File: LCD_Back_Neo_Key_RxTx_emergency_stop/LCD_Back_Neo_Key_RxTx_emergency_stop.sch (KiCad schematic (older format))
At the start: 12 parts, among them J1 Screw_Terminal_01x09, J2 Conn_01x20_Female, J3 Conn_01x08_Male, J4 Conn_01x01_Female, J5 Conn_01x01_Female, Q1 BC337, U1 DC-DC_Stepdown-Zimprich

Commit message: add new sheet 'Display'
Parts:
- removed C1: CP, Capacitor_THT:CP_Radial_D8.0mm_P2.50mm, symbol Device:CP
- removed J2: Conn_01x20_Female, Connector:LcdPinHeader, symbol LCD_Back_Neo_Key_RxTx_emergency_stop-rescue:Conn_01x20_LCD-Connector-ArduinoSig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
- removed Q1: BC337, Package_TO_SOT_THT:TO-92_Inline, symbol Transistor_BJT:BC337
- removed R1: R, Resistor_THT:R_Axial_DIN0207_L6.3mm_D2.5mm_P15.24mm_Horizontal, symbol Device:R
- removed R2: R, Resistor_THT:R_Axial_DIN0207_L6.3mm_D2.5mm_P10.16mm_Horizontal, symbol Device:R
- removed RL1: SONGLE_Relay_SRU-12VDC-SL-C, Relays_ThroughHole:Relay_SANYOU_SRD_Series_Form_C, symbol Zimprich:SONGLE_Relay_SRU-12VDC-SL-C
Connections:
- wire segments 60 -> 41
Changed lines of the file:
@@
 $Descr A4 11693 8268
 encoding utf-8
-Sheet 1 1
+Sheet 1 2
 Title ""
 Date "sam. 04 avril 2015"
@@
 	-1   0    0    1
 $EndComp
-$Comp
-L LCD_Back_Neo_Key_RxTx_emergency_stop-rescue:Conn_01x20_LCD-Connector-ArduinoSignalDriver-rescue J2
-U 1 1 5CE064F0
-P 9400 2150
-F 0 "J2" V 9565 2080 50  0000 C CNN
-F 1 "Conn_01x20_Female" V 9474 2080 50  0000 C CNN
-F 2 "Connector:LcdPinHeader" H 9400 2150 50  0001 C CNN
-F 3 "~" H 9400 2150 50  0001 C CNN
-	1    9400 2150
-	0    -1   -1   0
-$EndComp
-Text GLabel 10400 3550 3    50   Input ~ 0
-GND
-Text GLabel 10300 3550 3    50   Input ~ 0
-VCC-5V
-$Comp
-L Device:CP C1
-U 1 1 5CE0A632
-P 10200 4200
-F 0 "C1" H 10318 4246 50  0000 L CNN
-F 1 "CP" H 10318 4155 50  0000 L CNN
-F 2 "Capacitor_THT:CP_Radial_D8.0mm_P2.50mm" H 10238 4050 50  0001 C CNN
-F 3 "~" H 10200 4200 50  0001 C CNN
-	1    10200 4200
-	1    0    0    -1
-$EndComp
-$Comp
-L Device:R R1
-U 1 1 5CE0B53A
-P 9850 4050
-F 0 "R1" V 9643 4050 50  0000 C CNN
-F 1 "R" V 9734 4050 50  0000 C CNN
-F 2 "Resistor_THT:R_Axial_DIN0207_L6.3mm_D2.5mm_P15.24mm_Horizontal" V 9735 4050 50  0001 C CNN
-F 3 "~" H 9850 4050 50  0001 C CNN
-	1    9850 4050
-	0    1    1    0
-$EndComp
-Text GLabel 10200 4550 3    50   Input ~ 0
-GND
-Wire Wire Line
-	10200 4550 10200 4350
-Wire Wire Line
-	10000 4050 10200 4050
-Text GLabel 9500 4050 0    50   Input ~ 0
-Ardu_D3
-Wire Wire Line
-	9500 4050 9700 4050
 Wire Wire Line
 	5300 3100 5300 3650
@@
 Text GLabel 2200 4250 0    50   Input ~ 0
 GND
-$Comp
-L Transistor_BJT:BC337 Q1
-U 1 1 5CE3D215
-P 8400 4050
-F 0 "Q1" H 8591 4096 50  0000 L CNN
-F 1 "BC337" H 8591 4005 50  0000 L CNN
-F 2 "Package_TO_SOT_THT:TO-92_Inline" H 8600 3975 50  0001 L CIN
-F 3 "https://diotec.com/tl_files/diotec/files/pdf/datasheets/bc337.pdf" H 8400 4050 50  0001 L CNN
-	1    8400 4050
-	1    0    0    -1
-$EndComp
-$Comp
-L Device:R R2
-U 1 1 5CE41104
-P 7800 4050
-F 0 "R2" V 7593 4050 50  0000 C CNN
-F 1 "R" V 7684 4050 50  0000 C CNN
-F 2 "Resistor_THT:R_Axial_DIN0207_L6.3mm_D2.5mm_P10.16mm_Horizontal" V 7685 4050 50  0001 C CNN
-F 3 "~" H 7800 4050 50  0001 C CNN
-	1    7800 4050
-	0    1    1    0
-$EndComp
-Wire Wire Line
-	7950 4050 8200 4050
-Text GLabel 7350 4050 0    50   Input ~ 0
-Ardu_D5
-Wire Wire Line
-	7350 4050 7650 4050
-Text GLabel 8500 4350 3    50   Input ~ 0
-GND
-Wire Wire Line
-	8500 4350 8500 4250
-Wire Wire Line
-	8600 3400 10300 3400
-Wire Wire Line
-	10200 2350 10200 4050
-Connection ~ 10200 4050
-Wire Wire Line
-	8500 2350 8500 3850
-Wire Wire Line
-	10400 2350 10400 3300
-Connection ~ 10300 3400
-Wire Wire Line
-	10300 3400 10300 3550
-Wire Wire Line
-	10300 2350 10300 3400
-Wire Wire Line
-	8600 2350 8600 3400
-Wire Wire Line
-	9000 3300 10400 3300
-Wire Wire Line
-	9000 2350 9000 3300
-Connection ~ 10400 3300
-Wire Wire Line
-	10400 3300 10400 3550
 Text GLabel 6200 4650 2    50   Input ~ 0
 Ardu_A0
@@
 Wire Wire Line
 	4700 5350 4900 5350
-Text GLabel 10100 2550 3    50   Input ~ 0
-Ardu_A0
-Text GLabel 10000 2550 3    50   Input ~ 0
-Ardu_A1
-Text GLabel 9900 2550 3    50   Input ~ 0
-Ardu_D13
-Wire Wire Line
-	10100 2550 10100 2350
-Wire Wire Line
-	10000 2550 10000 2350
-Wire Wire Line
-	9900 2550 9900 2350
 Wire Wire Line
 	1050 4350 2350 4350
@@
 	1    0    0    -1
 $EndComp
-$Comp
-L Zimprich:SONGLE_Relay_SRU-12VDC-SL-C RL1
-U 1 1 5CE2CEAB
-P 3750 2300
-F 0 "RL1" H 4380 2546 50  0000 L CNN
-F 1 "SONGLE_Relay_SRU-12VDC-SL-C" H 4380 2455 50  0000 L CNN
-F 2 "Relays_ThroughHole:Relay_SANYOU_SRD_Series_Form_C" H 4400 2450 50  0001 L CNN
-F 3 "https://www.omron.com/ecb/products/pdf/en-g5q.pdf" H 3950 2100 50  0001 C CNN
-	1    3750 2300
-	1    0    0    -1
-$EndComp
+$Sheet
+S 9950 750  1050 250
+U 5CED8FBC
+F0 "Display" 50
+F1 "display.sch" 50
+$EndSheet
 $EndSCHEMATC

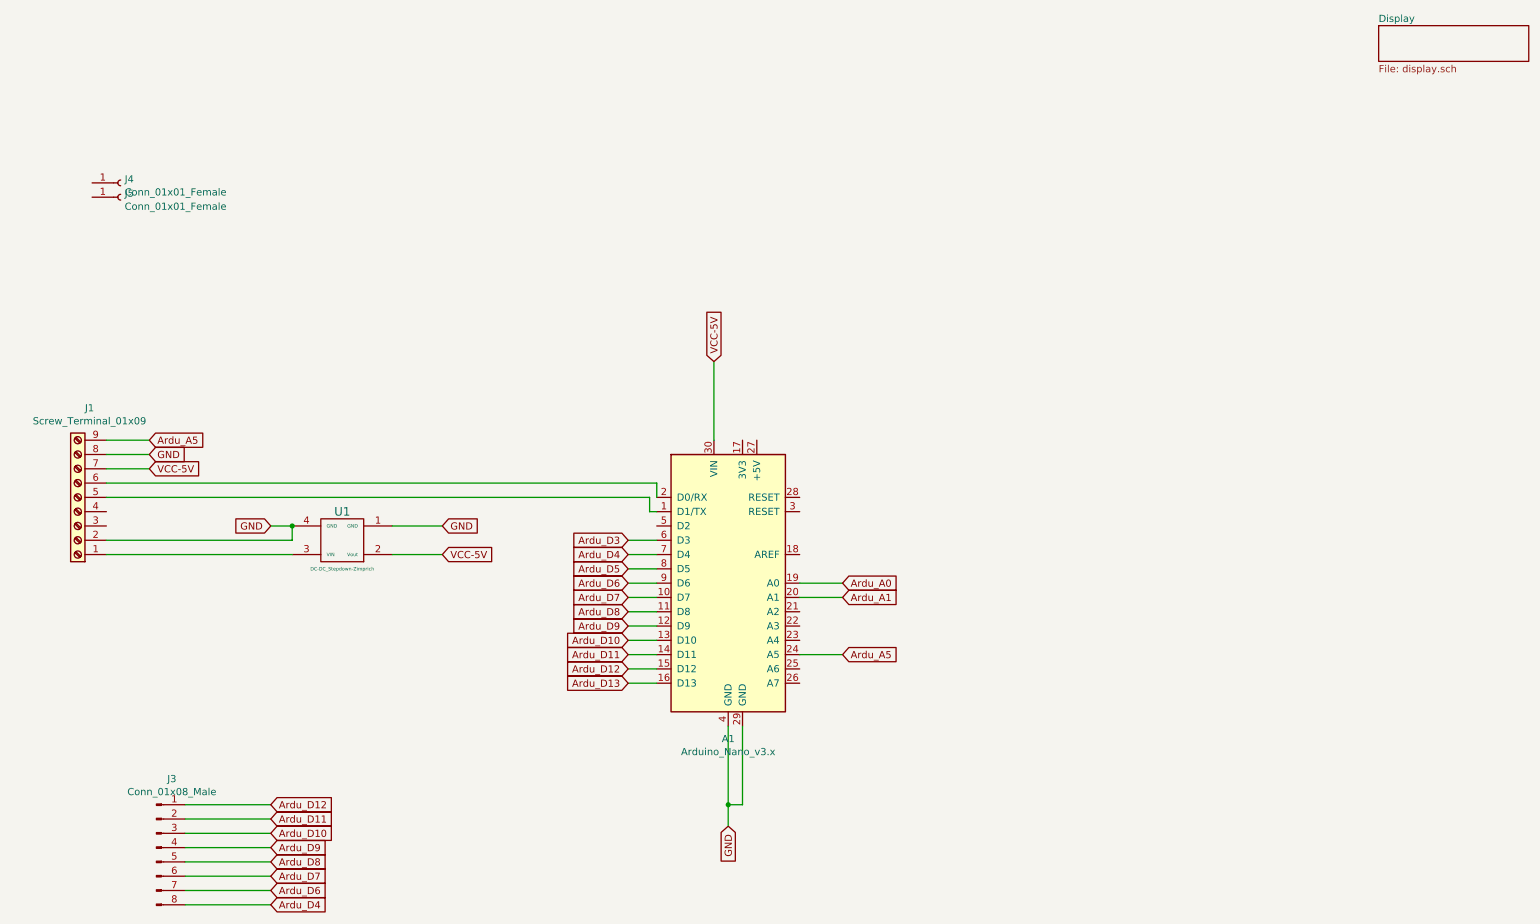
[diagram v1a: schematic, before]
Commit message: add sheet for emergency stop
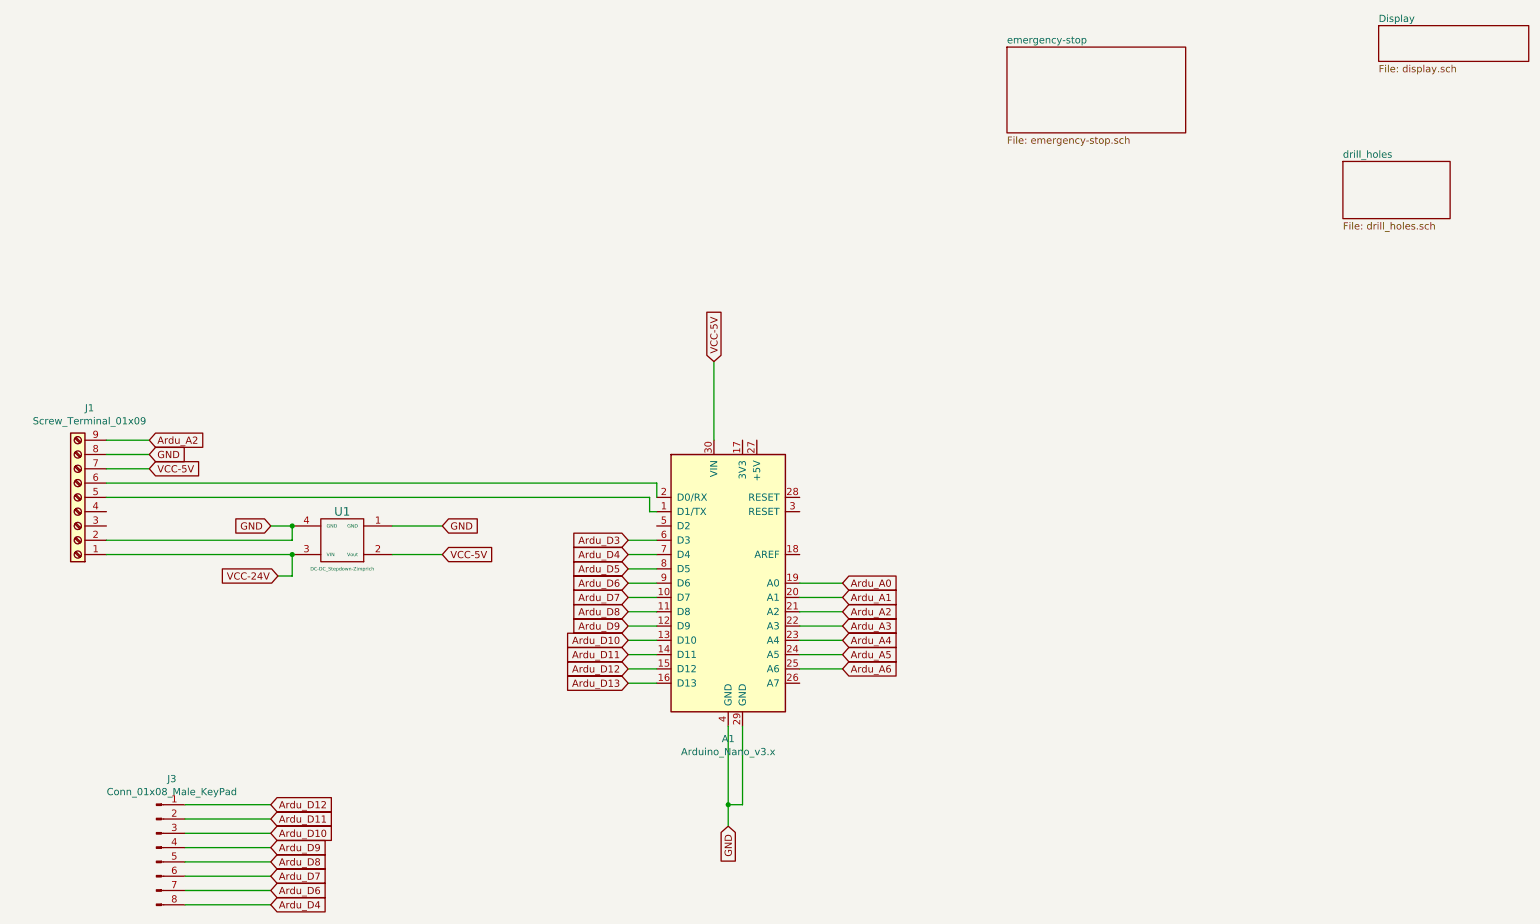
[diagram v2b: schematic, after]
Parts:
- removed J4, J5: Conn_01x01_Female, Connector_Pin:Pin_D0.7mm_L6.5mm_W1.8mm_FlatFork, symbol Connector:Conn_01x01_Female
- J3: value Conn_01x08_Male -> Conn_01x08_Male_KeyPad
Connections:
- net Ardu_A5: no longer J1.9 (Pin_9)
- net VCC-24V: now reaches J1.1 (Pin_1), U1.3 (VIN)
- net Ardu_A2: now reaches A1.21 (A2)
- net Ardu_A2: now also J1.9 (Pin_9)
- net Ardu_A3: now reaches A1.22 (A3)
- net Ardu_A4: now reaches A1.23 (A4)
- net Ardu_A6: now reaches A1.25 (A6)
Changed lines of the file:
@@
 $Descr A4 11693 8268
 encoding utf-8
-Sheet 1 2
+Sheet 1 4
 Title ""
 Date "sam. 04 avril 2015"
@@
 Wire Wire Line
 	5400 6200 5400 6350
-Text GLabel 6200 5150 2    50   Input ~ 0
-Ardu_A5
-Wire Wire Line
-	6200 5150 5900 5150
+Text GLabel 6200 4850 2    50   Input ~ 0
+Ardu_A2
 Text GLabel 1350 3650 2    50   Input ~ 0
-Ardu_A5
+Ardu_A2
 Wire Wire Line
 	1050 3650 1350 3650
@@
 P 1400 6500
 F 0 "J3" H 1508 6981 50  0000 C CNN
-F 1 "Conn_01x08_Male" H 1508 6890 50  0000 C CNN
+F 1 "Conn_01x08_Male_KeyPad" H 1508 6890 50  0000 C CNN
 F 2 "Connector_PinHeader_2.54mm:PinHeader_1x08_P2.54mm_Horizontal_invert" H 1400 6500 50  0001 C CNN
 F 3 "~" H 1400 6500 50  0001 C CNN
@@
 Wire Wire Line
 	4850 4050 1050 4050
-$Comp
-L Connector:Conn_01x01_Female J4
-U 1 1 5CE84571
-P 1150 1850
-F 0 "J4" H 1178 1876 50  0000 L CNN
-F 1 "Conn_01x01_Female" H 1178 1785 50  0000 L CNN
-F 2 "Connector_Pin:Pin_D0.7mm_L6.5mm_W1.8mm_FlatFork" H 1150 1850 50  0001 C CNN
-F 3 "~" H 1150 1850 50  0001 C CNN
-	1    1150 1850
-	1    0    0    -1
-$EndComp
-$Comp
-L Connector:Conn_01x01_Female J5
-U 1 1 5CE84B70
-P 1150 1950
-F 0 "J5" H 1178 1976 50  0000 L CNN
-F 1 "Conn_01x01_Female" H 1178 1885 50  0000 L CNN
-F 2 "Connector_Pin:Pin_D0.7mm_L6.5mm_W1.8mm_FlatFork" H 1150 1950 50  0001 C CNN
-F 3 "~" H 1150 1950 50  0001 C CNN
-	1    1150 1950
-	1    0    0    -1
-$EndComp
 $Sheet
 S 9950 750  1050 250
@@
 F1 "display.sch" 50
 $EndSheet
+Text GLabel 2250 4600 0    50   Input ~ 0
+VCC-24V
+Wire Wire Line
+	2250 4600 2350 4600
+Wire Wire Line
+	2350 4600 2350 4450
+Connection ~ 2350 4450
+$Sheet
+S 7350 900  1250 600
+U 5CED30A6
+F0 "emergency-stop" 50
+F1 "emergency-stop.sch" 50
+$EndSheet
+Wire Wire Line
+	6200 4850 5900 4850
+Text GLabel 6200 5050 2    50   Input ~ 0
+Ardu_A4
+Text GLabel 6200 5150 2    50   Input ~ 0
+Ardu_A5
+Wire Wire Line
+	6200 5050 5900 5050
+Wire Wire Line
+	6200 5150 5900 5150
+Text GLabel 6200 4950 2    50   Input ~ 0
+Ardu_A3
+Wire Wire Line
+	6200 4950 5900 4950
+$Sheet
+S 9700 1700 750  400
+U 5CF1B710
+F0 "drill_holes" 50
+F1 "drill_holes.sch" 50
+$EndSheet
+Text GLabel 6200 5250 2    50   Input ~ 0
+Ardu_A6
+Wire Wire Line
+	6200 5250 5900 5250
 $EndSCHEMATC

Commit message: combine screw terminal
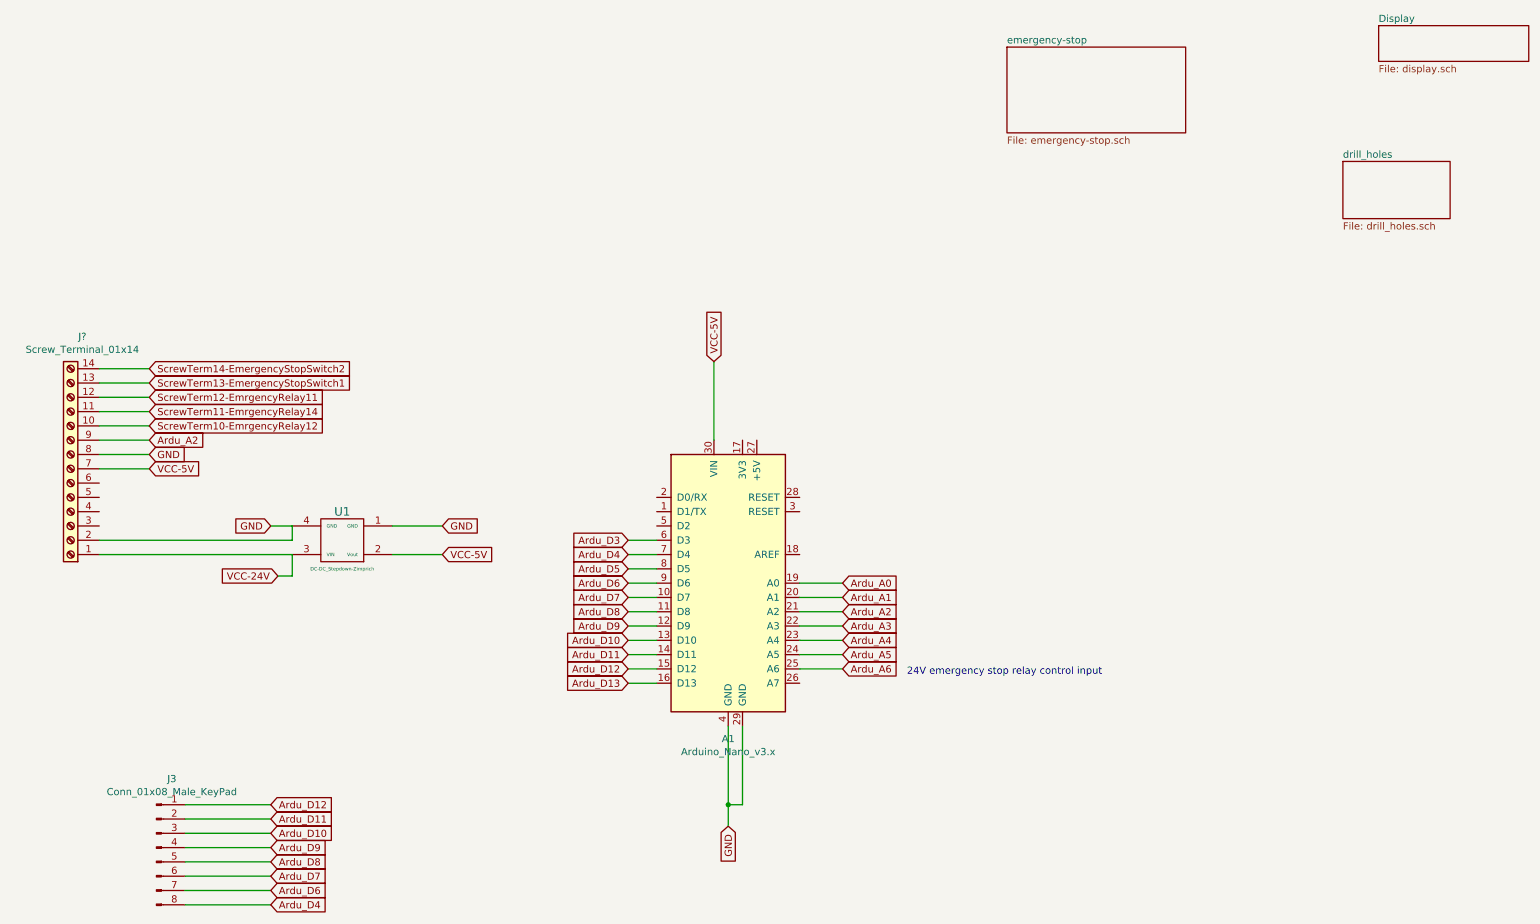
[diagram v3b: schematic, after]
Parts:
- removed J1: Screw_Terminal_01x09, TerminalBlock_Altech:Altech_AK300_1x09_P5.00mm_45-Degree, symbol Connector:Screw_Terminal_01x09
- added J?: Screw_Terminal_01x14, symbol Connector:Screw_Terminal_01x14
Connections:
- net Ardu_A2: now also J?.9 (Pin_9)
- net GND: now also J?.2 (Pin_2), J?.8 (Pin_8)
- net VCC-24V: now also J?.1 (Pin_1)
- net VCC-5V: now also J?.7 (Pin_7)
- new net ScrewTerm10-EmrgencyRelay12: J?.10 (Pin_10)
- new net ScrewTerm11-EmrgencyRelay14: J?.11 (Pin_11)
- new net ScrewTerm12-EmrgencyRelay11: J?.12 (Pin_12)
- new net ScrewTerm13-EmergencyStopSwitch1: J?.13 (Pin_13)
- new net ScrewTerm14-EmergencyStopSwitch2: J?.14 (Pin_14)
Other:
- note added: "24V emergency stop relay control input"
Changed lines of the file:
@@
 Wire Wire Line
 	3050 4450 3400 4450
-$Comp
-L Connector:Screw_Terminal_01x09 J1
-U 1 1 5CDFAC77
-P 850 4050
-F 0 "J1" H 768 3425 50  0000 C CNN
-F 1 "Screw_Terminal_01x09" H 768 3516 50  0000 C CNN
-F 2 "TerminalBlock_Altech:Altech_AK300_1x09_P5.00mm_45-Degree" H 850 4050 50  0001 C CNN
-F 3 "~" H 850 4050 50  0001 C CNN
-	1    850  4050
-	-1   0    0    1
-$EndComp
 Wire Wire Line
 	5300 3100 5300 3650
 Text GLabel 1350 3850 2    50   Input ~ 0
 VCC-5V
-Wire Wire Line
-	1350 3850 1050 3850
 Text GLabel 1350 3750 2    50   Input ~ 0
 GND
-Wire Wire Line
-	1350 3750 1050 3750
 Wire Wire Line
 	5400 6200 5500 6200
@@
 Text GLabel 1350 3650 2    50   Input ~ 0
 Ardu_A2
-Wire Wire Line
-	1050 3650 1350 3650
 $Comp
 L Connector:Conn_01x08_Male J3
@@
 Wire Wire Line
 	4900 4350 4700 4350
-Wire Wire Line
-	1050 4450 2350 4450
 Text GLabel 2200 4250 0    50   Input ~ 0
 GND
@@
 Wire Wire Line
 	4700 5350 4900 5350
-Wire Wire Line
-	1050 4350 2350 4350
 Wire Wire Line
 	2350 4350 2350 4250
@@
 Wire Wire Line
 	2200 4250 2350 4250
-Connection ~ 2350 4250
-Wire Wire Line
-	4900 4050 4900 3950
-Wire Wire Line
-	4900 3950 1050 3950
-Wire Wire Line
-	4900 4150 4850 4150
-Wire Wire Line
-	4850 4150 4850 4050
-Wire Wire Line
-	4850 4050 1050 4050
 $Sheet
 S 9950 750  1050 250
@@
 Wire Wire Line
 	2350 4600 2350 4450
-Connection ~ 2350 4450
 $Sheet
 S 7350 900  1250 600
@@
 Wire Wire Line
 	6200 5250 5900 5250
+$Comp
+L Connector:Screw_Terminal_01x14 J?
+U 1 1 5CEFB18C
+P 800 3850
+F 0 "J?" H 718 2925 50  0000 C CNN
+F 1 "Screw_Terminal_01x14" H 718 3016 50  0000 C CNN
+F 2 "" H 800 3850 50  0001 C CNN
+F 3 "~" H 800 3850 50  0001 C CNN
+	1    800  3850
+	-1   0    0    1
+$EndComp
+Wire Wire Line
+	1000 3650 1350 3650
+Wire Wire Line
+	1000 3750 1350 3750
+Wire Wire Line
+	1000 3850 1350 3850
+Wire Wire Line
+	1000 4350 2350 4350
+Wire Wire Line
+	1000 4450 2350 4450
+Text GLabel 1350 3550 2    50   Input ~ 0
+ScrewTerm10-EmrgencyRelay12
+Text GLabel 1350 3450 2    50   Input ~ 0
+ScrewTerm11-EmrgencyRelay14
+Text GLabel 1350 3350 2    50   Input ~ 0
+ScrewTerm12-EmrgencyRelay11
+Text GLabel 1350 3250 2    50   Input ~ 0
+ScrewTerm13-EmergencyStopSwitch1
+Text GLabel 1350 3150 2    50   Input ~ 0
+ScrewTerm14-EmergencyStopSwitch2
+Wire Wire Line
+	1350 3150 1000 3150
+Wire Wire Line
+	1350 3250 1000 3250
+Wire Wire Line
+	1350 3350 1000 3350
+Wire Wire Line
+	1350 3450 1000 3450
+Wire Wire Line
+	1350 3550 1000 3550
+Text Notes 6650 5300 0    50   ~ 0
+24V emergency stop relay control input
 $EndSCHEMATC

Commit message: update
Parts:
- A1: symbol MCU_Module:Arduino_Nano_v3.x -> LCD_Back_Neo_Key_RxTx_emergency_stop-rescue:Arduino_Nano_v3.x-MCU_Module
- J3: symbol Connector:Conn_01x08_Male -> LCD_Back_Neo_Key_RxTx_emergency_stop-rescue:Conn_01x08_Male-Connector
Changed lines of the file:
@@
 $EndDescr
 $Comp
-L MCU_Module:Arduino_Nano_v3.x A1
+L LCD_Back_Neo_Key_RxTx_emergency_stop-rescue:Arduino_Nano_v3.x-MCU_Module A1
 U 1 1 5CDFD485
 P 5400 4650
@@
 Ardu_A2
 $Comp
-L Connector:Conn_01x08_Male J3
+L LCD_Back_Neo_Key_RxTx_emergency_stop-rescue:Conn_01x08_Male-Connector J3
 U 1 1 5CE28136
 P 1400 6500

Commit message: place screwterminal on PCB
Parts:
- J1: renamed from J?; footprint (none) -> Connector_Phoenix_MSTB:PhoenixContact_MSTBVA_2,5_14-G_1x14_P5.00mm_Vertical
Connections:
- net ScrewTerm12-EmrgencyRelay11 is gone; now on net VCC-24V: J1.12 (Pin_12)
- net ScrewTerm13-EmergencyStopSwitch1 is gone; now on net GND: J1.13 (Pin_13)
- net Ardu_A2: now also J1.1 (Pin_1); no longer J1.9 (Pin_9)
- net Ardu_A4: now also J1.2 (Pin_2)
- net Ardu_A5: now also J1.3 (Pin_3)
- net GND: now also J1.4 (Pin_4); no longer J1.2 (Pin_2), J1.8 (Pin_8)
- net VCC-24V: no longer J1.1 (Pin_1)
- net VCC-5V: now also J1.5 (Pin_5); no longer J1.7 (Pin_7)
- net ScrewTerm8-EmrgencyRelay12: now reaches J1.6 (Pin_6)
- net ScrewTerm10-EmrgencyRelay12 renamed ScrewTerm12-EmergencyStopSwitch2
- net ScrewTerm11-EmrgencyRelay14 renamed ScrewTerm13-EmergencyStopSwitch3
- net ScrewTerm14-EmergencyStopSwitch2: no longer names the net of J1.14 (Pin_14)
- new net ScrewTerm10-EmrgencyRelay11: J1.8 (Pin_8)
- new net ScrewTerm11-EmergencyStopSwitch1: J1.9 (Pin_9)
- new net ScrewTerm9-EmrgencyRelay14: J1.7 (Pin_7)
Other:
- note added: "i2C SCL clock"
- note added: "i2C SDA data"
- note added: "neo pixel 5V"
- note added: "neo pixel GND"
- note added: "neo pixel IN"
- moved on the sheet: A1, J3, U1
